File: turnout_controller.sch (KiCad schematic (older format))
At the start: 21 parts, among them J1 DCC Input, J2 Servo Motor, J3 LED Connect

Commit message: Version 2: Passive components not yet defined.
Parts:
- added C7: 470u, c0603, symbol CAP_NP
- added SW1, SW2: SW_Push, symbol SW_Push
- D1: MFG (none) -> Comchip Technology; P/N (none) -> Z4GP208-HF
- D2: MFG (none) -> AVX; P/N (none) -> SD1206S020S1R0
- R2: value 4.7K -> 10K
- R4: renamed from R1; value 10K -> 4.7K
- R7: renamed from R3; MFG (none) -> Value; P/N (none) -> Value
- U1: renamed from U?; MFG (none) -> Diodes International; P/N (none) -> AP65111A
- U2: renamed from U?; MFG (none) -> NXP; P/N (none) -> MKE04P24M48SF0
- renumbered C4 to C1, C1 to C2, C5 to C3, C6 to C4, C2 to C5, C3 to C6, R4 to R1, R5 to R3, R7 to R5
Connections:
- net labels added: DCC_A, DCC_B, DCC_IN
- net labels removed: 5V_SUPPLY_OUT, DCC_NEG, DCC_POS
- wire segments 52 -> 72
- no-connect marks 0 -> 8
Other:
- note added: "5V SUPPLY"
- note added: "LED_1"
- note added: "LED_2"
- note added: "MOTOR_CNTL"
- note removed: "12V SUPPLY"
- note removed: "PWM MOTOR"
- note removed: "TO ANODE"
- note removed: "TO CATHODE"
- moved on the sheet: C1, C2, C3, C4, C5, C6, D1, D2, J1, J2, J3, L1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

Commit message: changed pushbuttons connectivity
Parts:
- removed SW2: SW_Push, symbol SW_Push
- added SW?: SW_Push, symbol SW_Push
- SW1: Label (none) -> \"UP\"
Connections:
- net labels added: KEY_DN, KEY_UP
- wire segments 72 -> 70
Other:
- moved on the sheet: SW1
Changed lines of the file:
@@
 LIBS:contrib
 LIBS:valves
-LIBS:teletram
-LIBS:tt-power
 LIBS:turnout_controller-cache
 EELAYER 25 0
@@
 	1    0    0    -1
 $EndComp
-Text Label 1650 1550 0    60   ~ 0
+Text Label 1700 1550 0    60   ~ 0
 DCC_A
-Text Label 1650 2350 0    60   ~ 0
+Text Label 1700 2350 0    60   ~ 0
 DCC_B
 $Comp
@@
 L SW_Push SW1
 U 1 1 5A1B3D6F
-P 6100 1450
-F 0 "SW1" H 5800 1600 50  0000 L CNN
-F 1 "SW_Push" H 6400 1600 50  0000 C CNN
-F 2 "" H 6100 1650 50  0001 C CNN
-F 3 "" H 6100 1650 50  0001 C CNN
-F 4 "ZJWin-Tech" H 6100 1450 60  0001 C CNN "MFG"
-F 5 "TS-1289VE-4" H 6100 1450 60  0001 C CNN "P/N"
-	1    6100 1450
-	1    0    0    -1
-$EndComp
-$Comp
-L SW_Push SW2
-U 1 1 5A1B3F90
-P 6100 1600
-F 0 "SW2" H 5800 1500 50  0000 L CNN
-F 1 "SW_Push" H 6400 1500 50  0000 C CNN
-F 2 "" H 6100 1800 50  0001 C CNN
-F 3 "" H 6100 1800 50  0001 C CNN
-F 4 "ZJWin-Tech" H 6100 1600 60  0001 C CNN "MFG"
-F 5 "TS-1289VE-4" H 6100 1600 60  0001 C CNN "P/N"
-	1    6100 1600
-	1    0    0    -1
-$EndComp
-Text Label 8300 1400 0    60   ~ 0
+P 7850 4000
+F 0 "SW1" H 7550 4050 50  0000 L CNN
+F 1 "SW_Push" H 7650 3950 50  0001 C CNN
+F 2 "" H 7850 4200 50  0001 C CNN
+F 3 "" H 7850 4200 50  0001 C CNN
+F 4 "ZJWin-Tech" H 7850 4000 60  0001 C CNN "MFG"
+F 5 "TS-1289VE-4" H 7850 4000 60  0001 C CNN "P/N"
+F 6 "\"UP\"" H 7850 4200 60  0000 C CNN "Label"
+	1    7850 4000
+	1    0    0    -1
+$EndComp
+Text Label 8100 1400 0    60   ~ 0
 DCC_IN
-Text Label 4050 1300 0    60   ~ 0
+Text Label 3850 1300 0    60   ~ 0
 DCC_IN
 $Comp
@@
 NoConn ~ 6750 1800
 NoConn ~ 6750 1900
-$Comp
-L 5V #PWR020
-U 1 1 5A1BA497
-P 5600 1250
-F 0 "#PWR020" H 5600 1350 40  0001 C CNN
-F 1 "5V" H 5600 1400 60  0000 C CNN
-F 2 "" H 5600 1250 60  0000 C CNN
-F 3 "" H 5600 1250 60  0000 C CNN
-	1    5600 1250
-	1    0    0    -1
-$EndComp
 Wire Wire Line
 	2500 1300 2500 1650
@@
 Connection ~ 2500 1550
 Wire Wire Line
-	7950 1400 8300 1400
+	7950 1400 8500 1400
 Wire Wire Line
 	3150 1300 3250 1300
 Wire Wire Line
-	3650 1300 4050 1300
+	3650 1300 4300 1300
 Wire Wire Line
 	3750 1300 3750 1400
@@
 Wire Wire Line
 	8700 2750 8700 2900
-Wire Wire Line
-	5600 1600 5900 1600
 Connection ~ 9350 1550
 Wire Wire Line
@@
 Connection ~ 9350 1900
 Wire Wire Line
-	5600 1450 5900 1450
-Wire Wire Line
-	6300 1450 6500 1450
-Wire Wire Line
-	6500 1450 6500 1400
-Wire Wire Line
-	6500 1400 6750 1400
-Wire Wire Line
-	6300 1600 6550 1600
-Wire Wire Line
-	6550 1600 6550 1500
-Wire Wire Line
-	6550 1500 6750 1500
+	6350 1500 6750 1500
 Wire Wire Line
 	2800 1950 3000 1950
@@
 Connection ~ 9350 1300
 Wire Wire Line
-	5600 1250 5600 1600
-Connection ~ 5600 1450
-Wire Wire Line
 	1850 4250 1800 4250
 Wire Wire Line
 	2250 4250 2350 4250
+Wire Wire Line
+	6750 1400 6350 1400
+Text Label 6400 1400 0    60   ~ 0
+KEY_UP
+Text Label 6400 1500 0    60   ~ 0
+KEY_DN
+Wire Wire Line
+	8050 4300 8450 4300
+Wire Wire Line
+	8450 4000 8050 4000
+Text Label 8100 4000 0    60   ~ 0
+KEY_UP
+Text Label 8100 4300 0    60   ~ 0
+KEY_DN
+$Comp
+L SW_Push SW?
+U 1 1 5A1C72E9
+P 7850 4300
+F 0 "SW?" H 7550 4350 50  0000 L CNN
+F 1 "SW_Push" H 7650 4250 50  0001 C CNN
+F 2 "" H 7850 4500 50  0001 C CNN
+F 3 "" H 7850 4500 50  0001 C CNN
+F 4 "ZJWin-Tech" H 7850 4300 60  0001 C CNN "MFG"
+F 5 "TS-1289VE-4" H 7850 4300 60  0001 C CNN "P/N"
+F 6 "\"DOWN\"" H 7850 4200 60  0000 C CNN "Label"
+	1    7850 4300
+	1    0    0    -1
+$EndComp
+Wire Wire Line
+	7650 4000 7450 4000
+Wire Wire Line
+	7450 4000 7450 4400
+Wire Wire Line
+	7650 4300 7450 4300
+Connection ~ 7450 4300
+$Comp
+L GND_ #PWR?
+U 1 1 5A1C74FD
+P 7450 4450
+F 0 "#PWR?" H 7550 4550 30  0001 C CNN
+F 1 "GND_" H 7450 4350 30  0001 C CNN
+F 2 "" H 7450 4450 60  0000 C CNN
+F 3 "" H 7450 4450 60  0000 C CNN
+	1    7450 4450
+	1    0    0    -1
+$EndComp
 $EndSCHEMATC

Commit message: Corrected LED Resistor value and added note. Rearranged schematic
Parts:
- R7: value 470 -> 1k
- gave numbers to parts that had none: 1
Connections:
- wire segments 70 -> 68
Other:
- note added: "R7 calculated for 5mA (Imax/pin)\n5V Output\n25% Intensity based on HT-191TW\n"
- moved on the sheet: C1, C2, C3, C4, D1, D2, J1, L1, R1, R2, R3, R4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

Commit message: Updated turnout controller
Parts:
- C7: value 470u -> 22u
- D1: MFG Comchip Technology -> (none); MFG P/N (none) -> Z4GP208-HF; P/N Z4GP208-HF -> (none)
- R7: value 1k -> 380
- U1: MFG Diodes International -> (none); MFG P/N (none) -> AP65111A; P/N AP65111A -> (none)
- U2: symbol MKE04P24M48SF0 -> MKE04P24M48SF0-RESCUE-turnout_controller; MFG NXP -> (none); MFG P/N (none) -> MKE04P24M48SF0; P/N MKE04P24M48SF0 -> (none)
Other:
- note added: "R7 calculated for 5mA (Imax/pin)\n5V output, 3.1V drop\n25% Intensity based on HT-191TW\n"
- note removed: "R7 calculated for 5mA (Imax/pin)\n5V Output\n25% Intensity based on HT-191TW\n"
- moved on the sheet: C1, C3, C4, D2, L1, R1, R2, R3, R4, R5, R6, U1

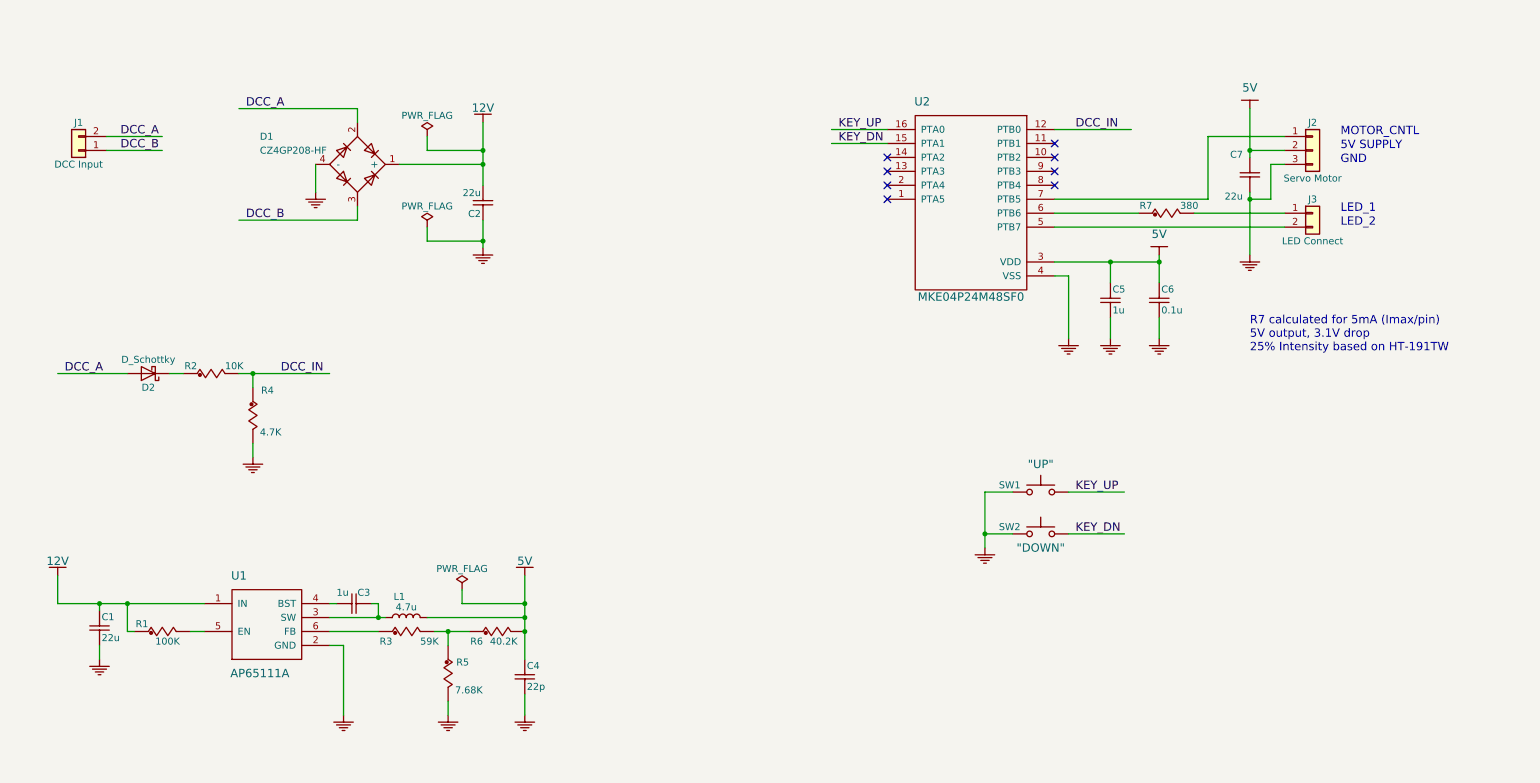
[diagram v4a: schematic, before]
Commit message: 
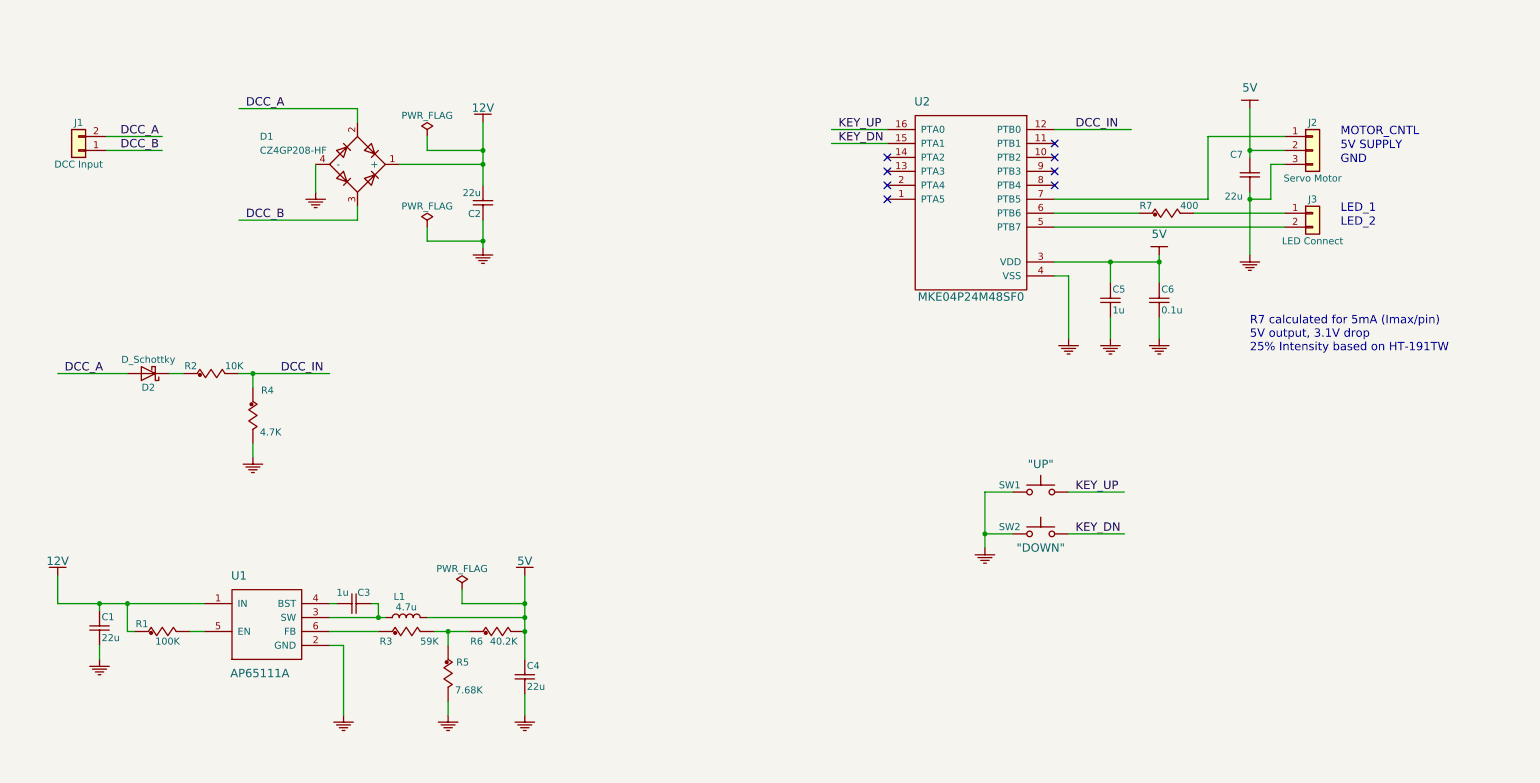
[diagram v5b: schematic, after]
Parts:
- C4: value 22p -> 22u
- D2: footprint (none) -> 1206; MFG AVX -> (none); MFG P/N (none) -> SD1206S020S1R0; P/N SD1206S020S1R0 -> (none)
- L1: footprint (none) -> 3012; MFG P/N (none) -> NRH3012T4R7MN
- R7: value 380 -> 400
- SW1: MFG ZJWin-Tech -> (none); MFG P/N (none) -> TS-1289VE-4; P/N TS-1289VE-4 -> (none)
- U1: footprint (none) -> TSOT26
- U2: footprint (none) -> TSSOP16
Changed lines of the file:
@@
 F 0 "L1" V 3450 4950 50  0000 C CNN
 F 1 "4.7u" V 3375 4900 50  0000 C CNN
-F 2 "" H 3300 4900 50  0001 C CNN
+F 2 "3012" H 3300 4900 50  0001 C CNN
 F 3 "" H 3300 4900 50  0001 C CNN
+F 4 "NRH3012T4R7MN" V 3300 4900 60  0001 C CNN "MFG P/N"
 	1    3300 4900
 	0    -1   -1   0
@@
 P 4150 5450
 F 0 "C4" H 4165 5625 50  0000 L BNN
-F 1 "22p" H 4165 5475 50  0000 L BNN
+F 1 "22u" H 4165 5475 50  0000 L BNN
 F 2 "c0603" H 4225 5350 40  0001 L BNN
 F 3 "" H 4150 5450 60  0000 C CNN
@@
 F 0 "U2" H 7000 4000 60  0000 C CNN
 F 1 "MKE04P24M48SF0" H 7350 2600 60  0000 C CNN
-F 2 "" H 7350 2600 60  0001 C CNN
+F 2 "TSSOP16" H 7350 2600 60  0001 C CNN
 F 3 "" H 7350 2600 60  0001 C CNN
 F 4 "MKE04P24M48SF0" H 7350 2600 60  0001 C CNN "MFG P/N"
@@
 F 0 "U1" H 2100 5800 60  0000 C CNN
 F 1 "AP65111A" H 2250 5100 60  0000 C CNN
-F 2 "" H 2250 5200 60  0001 C CNN
+F 2 "TSOT26" H 2250 5200 60  0001 C CNN
 F 3 "" H 2250 5200 60  0001 C CNN
 F 4 "AP65111A" H 2250 5200 60  0001 C CNN "MFG P/N"
@@
 P 8550 2050
 F 0 "R7" H 8650 2125 50  0000 R BNN
-F 1 "380" H 8850 2125 50  0000 L BNN
+F 1 "400" H 8850 2125 50  0000 L BNN
 F 2 "r0603" H 8650 2000 40  0001 L BNN
 F 3 "" H 8550 2050 60  0000 C CNN
@@
 F 0 "D2" H 1450 3250 50  0000 C CNN
 F 1 "D_Schottky" H 1450 3050 50  0000 C CNN
-F 2 "" H 1450 3150 50  0001 C CNN
+F 2 "1206" H 1450 3150 50  0001 C CNN
 F 3 "" H 1450 3150 50  0001 C CNN
-F 4 "AVX" H 1450 3150 60  0001 C CNN "MFG"
-F 5 "SD1206S020S1R0" H 1450 3150 60  0001 C CNN "P/N"
+F 4 "SD1206S020S1R0" H 1450 3150 60  0001 C CNN "MFG P/N"
 	1    1450 3150
 	-1   0    0    1
@@
 F 2 "" H 7850 4200 50  0001 C CNN
 F 3 "" H 7850 4200 50  0001 C CNN
-F 4 "ZJWin-Tech" H 7850 4000 60  0001 C CNN "MFG"
-F 5 "TS-1289VE-4" H 7850 4000 60  0001 C CNN "P/N"
-F 6 "\"UP\"" H 7850 4200 60  0000 C CNN "Label"
+F 4 "TS-1289VE-4" H 7850 4000 60  0001 C CNN "MFG P/N"
+F 5 "\"UP\"" H 7850 4200 60  0000 C CNN "Label"
 	1    7850 4000
 	1    0    0    -1
@@
 $EndComp
 $Comp
-L PWR_FLAG #FLG018
+L PWR_FLAG #FLG017
 U 1 1 5A1B89B5
 P 3450 1450
-F 0 "#FLG018" H 3450 1525 50  0001 C CNN
+F 0 "#FLG017" H 3450 1525 50  0001 C CNN
 F 1 "PWR_FLAG" H 3450 1600 50  0000 C CNN
 F 2 "" H 3450 1450 50  0001 C CNN
@@
 	8350 2350 8350 2500
 Wire Wire Line
-	9350 1250 9350 1600
-Wire Wire Line
 	8700 2300 8700 2500
 Wire Wire Line
@@
 Wire Wire Line
 	8700 2750 8700 2900
-Connection ~ 9350 1550
 Wire Wire Line
 	9350 1850 9350 2300
 Wire Wire Line
 	9500 1650 9600 1650
-Wire Wire Line
-	9600 1550 9350 1550
 Wire Wire Line
 	9050 1900 9050 1450
@@
 Connection ~ 7450 4300
 $Comp
-L GND_ #PWR019
+L GND_ #PWR018
 U 1 1 5A1C74FD
 P 7450 4450
-F 0 "#PWR019" H 7550 4550 30  0001 C CNN
+F 0 "#PWR018" H 7550 4550 30  0001 C CNN
 F 1 "GND_" H 7450 4350 30  0001 C CNN
 F 2 "" H 7450 4450 60  0000 C CNN
@@
 Connection ~ 3850 2200
 $Comp
-L PWR_FLAG #FLG020
+L PWR_FLAG #FLG019
 U 1 1 5A1E3C8A
 P 3700 4700
-F 0 "#FLG020" H 3700 4775 50  0001 C CNN
+F 0 "#FLG019" H 3700 4775 50  0001 C CNN
 F 1 "PWR_FLAG" H 3700 4850 50  0000 C CNN
 F 2 "" H 3700 4700 50  0001 C CNN
@@
 R7 calculated for 5mA (Imax/pin)\n5V output, 3.1V drop\n25% Intensity based on HT-191TW\n
 $Comp
-L PWR_FLAG #FLG?
+L PWR_FLAG #FLG020
 U 1 1 5A2309DE
 P 3450 2100
-F 0 "#FLG?" H 3450 2175 50  0001 C CNN
+F 0 "#FLG020" H 3450 2175 50  0001 C CNN
 F 1 "PWR_FLAG" H 3450 2250 50  0000 C CNN
 F 2 "" H 3450 2100 50  0001 C CNN
@@
 	1    0    0    -1
 $EndComp
+Wire Wire Line
+	9350 1250 9350 1600
+Wire Wire Line
+	9600 1550 9350 1550
+Connection ~ 9350 1550
 $EndSCHEMATC

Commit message: Includes:
New project file
Footprints for buttons, bridge rectifier and edge connectors
initial circuit board layout
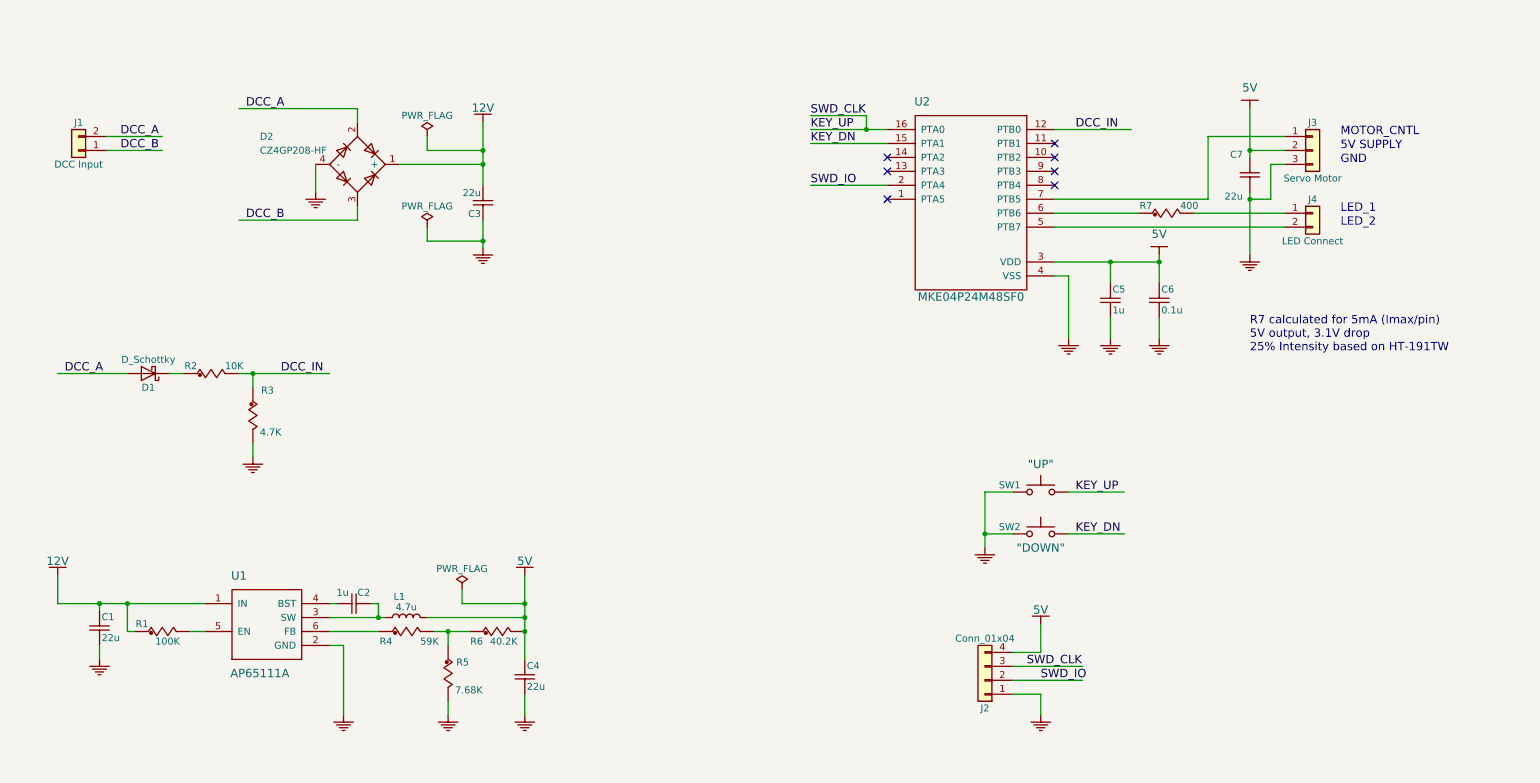
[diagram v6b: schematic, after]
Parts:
- added J2: Conn_01x04, Socket_Strips:Socket_Strip_Straight_1x04_Pitch1.27mm, symbol Conn_01x04
- C1, C4, C5, C6, C7: footprint c0603 -> Capacitors_SMD:C_0603_HandSoldering
- C2: renamed from C3; footprint c0603 -> Capacitors_SMD:C_0603_HandSoldering
- C3: renamed from C2; footprint c0603 -> Capacitors_SMD:C_0603_HandSoldering
- D1: renamed from D2; footprint 1206 -> Diodes_SMD:D_SOD-523
- D2: renamed from D1; footprint (none) -> Z4GP208-HF:Z4GP208-HF-SMD
- J1: footprint (none) -> Socket_Strips:Socket_Strip_Straight_1x02_Pitch1.27mm
- J3: renamed from J2; footprint (none) -> Socket_Strips:Socket_Strip_Straight_1x03_Pitch1.27mm
- J4: renamed from J3; footprint (none) -> Socket_Strips:Socket_Strip_Straight_1x02_Pitch1.27mm
- L1: footprint 3012 -> Inductors_SMD:L_Taiyo-Yuden_NR-30xx
- R1, R2, R5, R6, R7: footprint r0603 -> Resistors_SMD:R_0603_HandSoldering
- R3: renamed from R4; footprint r0603 -> Resistors_SMD:R_0603_HandSoldering
- R4: renamed from R3; footprint r0603 -> Resistors_SMD:R_0603_HandSoldering
- SW1, SW2: footprint (none) -> tt_buttons:HTB1-Button
- U1: footprint TSOT26 -> TO_SOT_Packages_SMD:SOT-23-6
- U2: footprint TSSOP16 -> Housings_SSOP:TSSOP-16_4.4x5mm_Pitch0.65mm
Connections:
- net labels added: SWD_CLK, SWD_IO
- wire segments 68 -> 77
- no-connect marks 8 -> 7
